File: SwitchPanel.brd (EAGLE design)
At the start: 101.6 x 30.5 mm, 16 parts

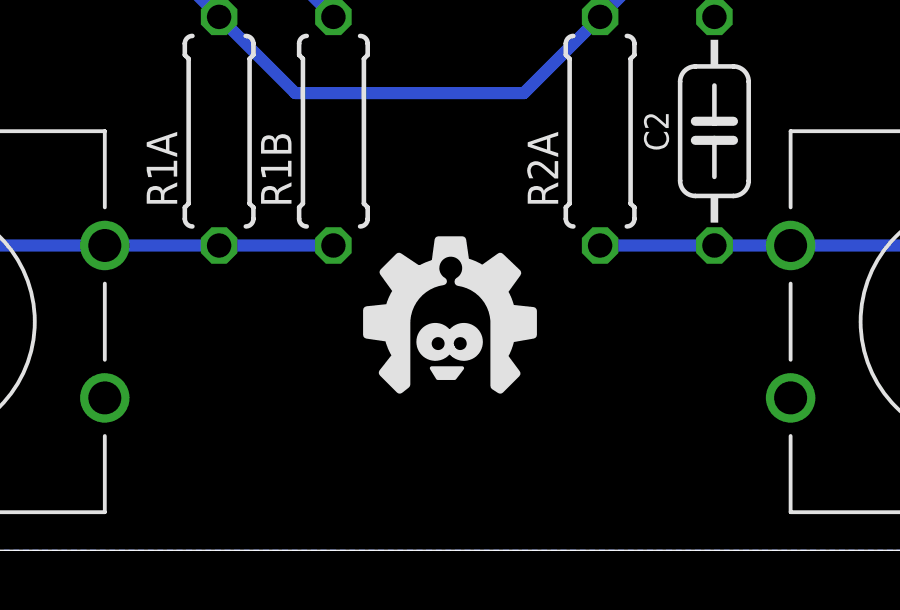
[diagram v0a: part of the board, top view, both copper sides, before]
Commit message: Moved logo to bottom silk
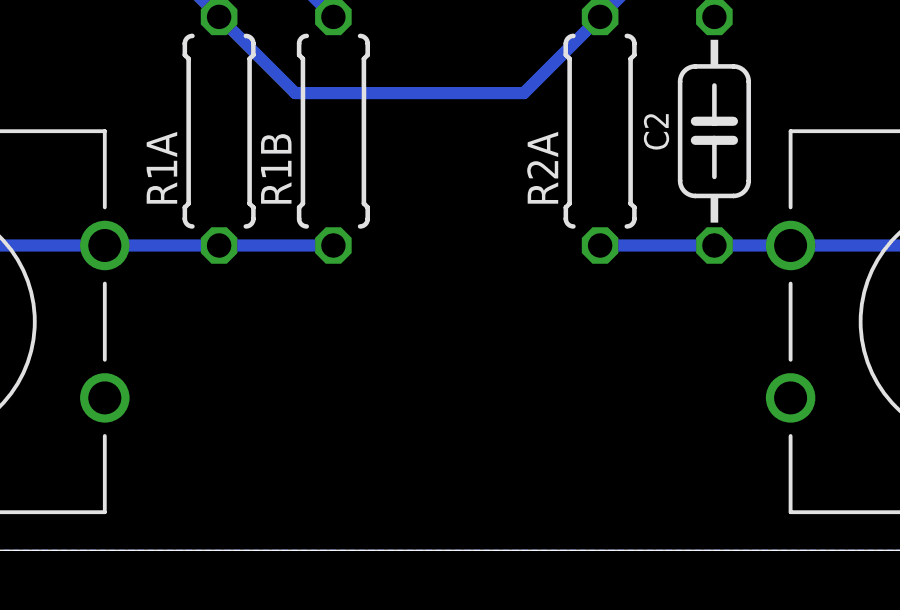
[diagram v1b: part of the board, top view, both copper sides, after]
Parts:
- flipped U$4 to the bottom
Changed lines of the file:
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@@
 <element name="S2" library="bt_electromech" package="12MMTACTILE_4PIN" value="" x="50.8" y="7.62"/>
 <element name="S3" library="bt_electromech" package="12MMTACTILE_4PIN" value="" x="86.36" y="7.62"/>
-<element name="U$4" library="bt" package="BTLOGOM" value="" x="33.02" y="5.08"/>
+<element name="U$4" library="bt" package="BTLOGOM" value="" x="33.02" y="5.08" rot="MR0"/>
 </elements>
 <signals>
